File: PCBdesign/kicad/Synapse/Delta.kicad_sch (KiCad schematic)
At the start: 12 parts, among them IC1 ALD1105PBL, P4 TSW-102-07-G-S

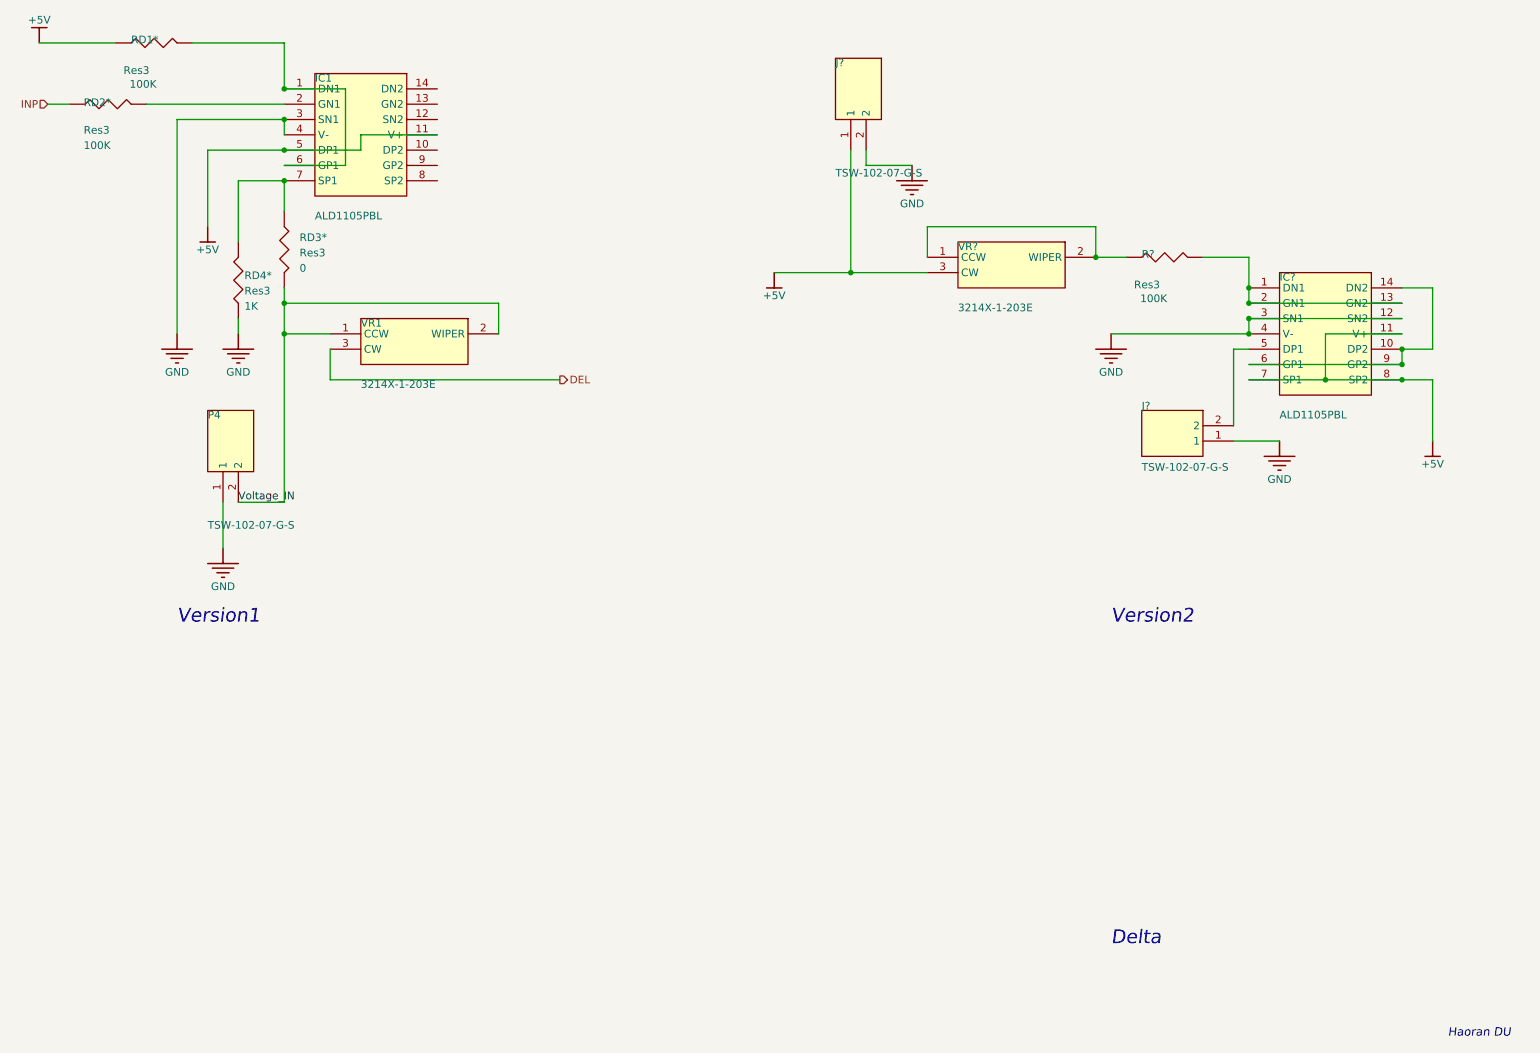
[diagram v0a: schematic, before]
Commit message: Annotate schematics (auto via kicad) and generate netlists.
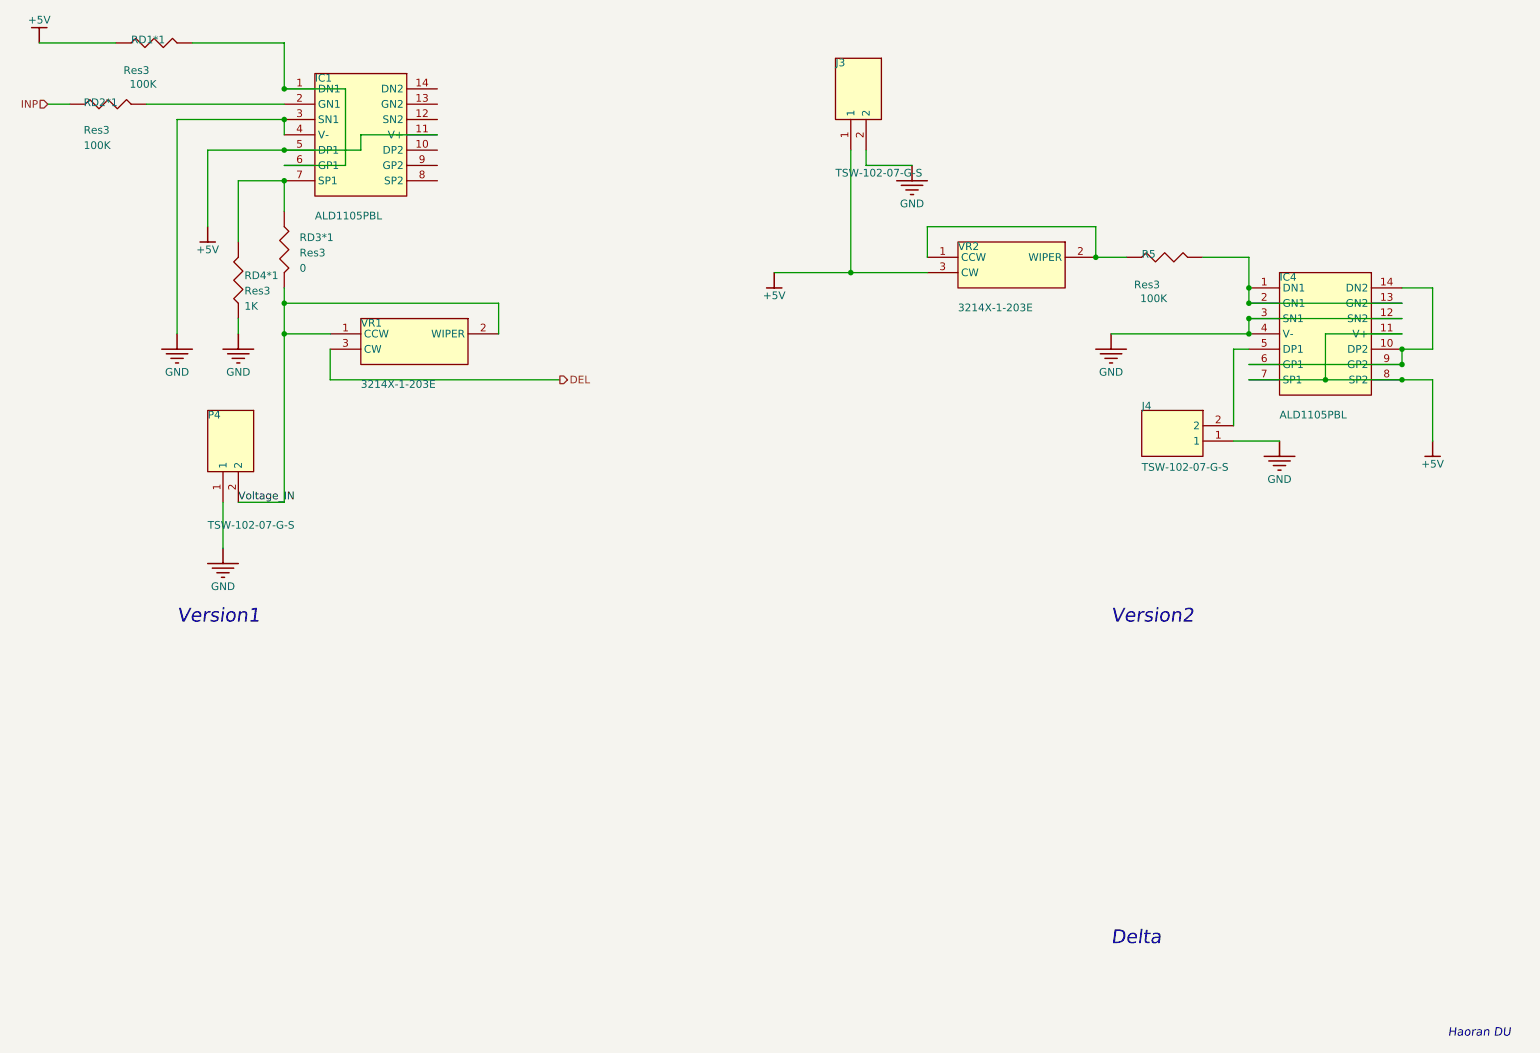
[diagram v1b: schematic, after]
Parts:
- gave numbers to parts that had none: 5
- renumbered RD1* to RD1*1, RD2* to RD2*1, RD3* to RD3*1, RD4* to RD4*1
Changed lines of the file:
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@@
 		(in_pos_files yes)
 		(dnp no)
-		(property "Reference" "#PWR?"
+		(property "Reference" "#PWR03"
 			(at 55.88 70.3072 0)
 			(hide yes)
@@
 			(project "Synapse_LPS"
 				(path "/af4a7426-c915-4fd8-a9a0-d1d0653890c7/984ef279-a542-4986-b306-8a6747a54659"
-					(reference "#PWR?")
+					(reference "#PWR03")
 					(unit 1)
 				)
@@
 		(in_pos_files yes)
 		(dnp no)
-		(property "Reference" "#PWR?"
+		(property "Reference" "#PWR06"
 			(at 149.86 77.9272 0)
 			(hide yes)
@@
 			(project "Synapse_LPS"
 				(path "/af4a7426-c915-4fd8-a9a0-d1d0653890c7/984ef279-a542-4986-b306-8a6747a54659"
-					(reference "#PWR?")
+					(reference "#PWR06")
 					(unit 1)
 				)
@@
 		(in_pos_files yes)
 		(dnp no)
-		(property "Reference" "RD1*"
+		(property "Reference" "RD1*1"
 			(at 43.18 38.5572 90)
 			(show_name no)
@@
 			(project "Synapse_LPS"
 				(path "/af4a7426-c915-4fd8-a9a0-d1d0653890c7/984ef279-a542-4986-b306-8a6747a54659"
-					(reference "RD1*")
+					(reference "RD1*1")
 					(unit 1)
 				)
@@
 		(in_pos_files yes)
 		(dnp no)
-		(property "Reference" "RD3*"
+		(property "Reference" "RD3*1"
 			(at 71.12 72.8472 0)
 			(show_name no)
@@
 			(project "Synapse_LPS"
 				(path "/af4a7426-c915-4fd8-a9a0-d1d0653890c7/984ef279-a542-4986-b306-8a6747a54659"
-					(reference "RD3*")
+					(reference "RD3*1")
 					(unit 1)
 				)
@@
 		(in_pos_files yes)
 		(dnp no)
-		(property "Reference" "#PWR?"
+		(property "Reference" "#PWR04"
 			(at 58.42 123.6472 0)
 			(hide yes)
@@
 			(project "Synapse_LPS"
 				(path "/af4a7426-c915-4fd8-a9a0-d1d0653890c7/984ef279-a542-4986-b306-8a6747a54659"
-					(reference "#PWR?")
+					(reference "#PWR04")
 					(unit 1)
 				)
@@
 		(in_pos_files yes)
 		(dnp no)
-		(property "Reference" "RD4*"
+		(property "Reference" "RD4*1"
 			(at 61.976 77.6732 0)
 			(show_name no)
@@
 			(project "Synapse_LPS"
 				(path "/af4a7426-c915-4fd8-a9a0-d1d0653890c7/984ef279-a542-4986-b306-8a6747a54659"
-					(reference "RD4*")
+					(reference "RD4*1")
 					(unit 1)
 				)
@@
 		(in_pos_files yes)
 		(dnp no)
-		(property "Reference" "#PWR?"
+		(property "Reference" "#PWR07"
 			(at 172.72 60.1472 0)
 			(hide yes)
@@
 			(project "Synapse_LPS"
 				(path "/af4a7426-c915-4fd8-a9a0-d1d0653890c7/984ef279-a542-4986-b306-8a6747a54659"
-					(reference "#PWR?")
+					(reference "#PWR07")
 					(unit 1)
 				)
@@
 		(in_pos_files yes)
 		(dnp no)
-		(property "Reference" "R?"
+		(property "Reference" "R5"
 			(at 210.82 74.1172 90)
 			(show_name no)
@@
 			(project "Synapse_LPS"
 				(path "/af4a7426-c915-4fd8-a9a0-d1d0653890c7/984ef279-a542-4986-b306-8a6747a54659"
-					(reference "R?")
+					(reference "R5")
 					(unit 1)
 				)
@@
 		(in_pos_files yes)
 		(dnp no)
-		(property "Reference" "IC?"
+		(property "Reference" "IC4"
 			(at 233.68 77.9272 90)
 			(show_name no)
@@
 			(project "Synapse_LPS"
 				(path "/af4a7426-c915-4fd8-a9a0-d1d0653890c7/984ef279-a542-4986-b306-8a6747a54659"
-					(reference "IC?")
+					(reference "IC4")
 					(unit 1)
 				)
@@
 		(in_pos_files yes)
 		(dnp no)
-		(property "Reference" "#PWR?"
+		(property "Reference" "#PWR05"
 			(at 60.96 88.0872 0)
 			(hide yes)
@@
 			(project "Synapse_LPS"
 				(path "/af4a7426-c915-4fd8-a9a0-d1d0653890c7/984ef279-a542-4986-b306-8a6747a54659"
-					(reference "#PWR?")
+					(reference "#PWR05")
 					(unit 1)
 				)
@@
 		(in_pos_files yes)
 		(dnp no)
-		(property "Reference" "RD2*"
+		(property "Reference" "RD2*1"
 			(at 35.306 48.9712 90)
 			(show_name no)
@@
 			(project "Synapse_LPS"
 				(path "/af4a7426-c915-4fd8-a9a0-d1d0653890c7/984ef279-a542-4986-b306-8a6747a54659"
-					(reference "RD2*")
+					(reference "RD2*1")
 					(unit 1)
 				)
@@
 		(in_pos_files yes)
 		(dnp no)
-		(property "Reference" "#PWR?"
+		(property "Reference" "#PWR01"
 			(at 27.94 39.8272 0)
 			(hide yes)
@@
 			(project "Synapse_LPS"
 				(path "/af4a7426-c915-4fd8-a9a0-d1d0653890c7/984ef279-a542-4986-b306-8a6747a54659"
-					(reference "#PWR?")
+					(reference "#PWR01")
 					(unit 1)
 				)
@@
 		(in_pos_files yes)
 		(dnp no)
-		(property "Reference" "#PWR?"
+		(property "Reference" "#PWR08"
 			(at 205.74 88.0872 0)
 			(hide yes)
@@
 			(project "Synapse_LPS"
 				(path "/af4a7426-c915-4fd8-a9a0-d1d0653890c7/984ef279-a542-4986-b306-8a6747a54659"
-					(reference "#PWR?")
+					(reference "#PWR08")
 					(unit 1)
 				)
@@
 		(in_pos_files yes)
 		(dnp no)
-		(property "Reference" "VR?"
+		(property "Reference" "VR2"
 			(at 180.34 72.8472 90)
 			(show_name no)
@@
 			(project "Synapse_LPS"
 				(path "/af4a7426-c915-4fd8-a9a0-d1d0653890c7/984ef279-a542-4986-b306-8a6747a54659"
-					(reference "VR?")
+					(reference "VR2")
 					(unit 1)
 				)
@@
 		(in_pos_files yes)
 		(dnp no)
-		(property "Reference" "#PWR?"
+		(property "Reference" "#PWR010"
 			(at 259.08 105.8672 0)
 			(hide yes)
@@
 			(project "Synapse_LPS"
 				(path "/af4a7426-c915-4fd8-a9a0-d1d0653890c7/984ef279-a542-4986-b306-8a6747a54659"
-					(reference "#PWR?")
+					(reference "#PWR010")
 					(unit 1)
 				)
@@
 		(in_pos_files yes)
 		(dnp no)
-		(property "Reference" "J?"
+		(property "Reference" "J4"
 			(at 210.82 100.7872 90)
 			(show_name no)
@@
 			(project "Synapse_LPS"
 				(path "/af4a7426-c915-4fd8-a9a0-d1d0653890c7/984ef279-a542-4986-b306-8a6747a54659"
-					(reference "J?")
+					(reference "J4")
 					(unit 1)
 				)
@@
 		(in_pos_files yes)
 		(dnp no)
-		(property "Reference" "J?"
+		(property "Reference" "J3"
 			(at 160.02 42.3672 0)
 			(show_name no)
@@
 			(project "Synapse_LPS"
 				(path "/af4a7426-c915-4fd8-a9a0-d1d0653890c7/984ef279-a542-4986-b306-8a6747a54659"
-					(reference "J?")
+					(reference "J3")
 					(unit 1)
 				)
@@
 		(in_pos_files yes)
 		(dnp no)
-		(property "Reference" "#PWR?"
+		(property "Reference" "#PWR09"
 			(at 233.68 105.8672 0)
 			(hide yes)
@@
 			(project "Synapse_LPS"
 				(path "/af4a7426-c915-4fd8-a9a0-d1d0653890c7/984ef279-a542-4986-b306-8a6747a54659"
-					(reference "#PWR?")
+					(reference "#PWR09")
 					(unit 1)
 				)
@@
 		(in_pos_files yes)
 		(dnp no)
-		(property "Reference" "#PWR?"
+		(property "Reference" "#PWR02"
 			(at 50.8 88.0872 0)
 			(hide yes)
@@
 			(project "Synapse_LPS"
 				(path "/af4a7426-c915-4fd8-a9a0-d1d0653890c7/984ef279-a542-4986-b306-8a6747a54659"
-					(reference "#PWR?")
+					(reference "#PWR02")
 					(unit 1)
 				)
